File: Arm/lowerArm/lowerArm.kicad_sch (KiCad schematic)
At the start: 4 parts, among them J1 Screw_Terminal_01x12, J2 Screw_Terminal_01x12, U1 LM1084-5.0

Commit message: updated Arm arduino code, manual_operate, and PCBs
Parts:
- added C1: 0.1uF, Capacitor_SMD:C_0805_2012Metric, symbol Device:C_Small
- added C2, C3: 22pF, Capacitor_SMD:C_0805_2012Metric, symbol Device:C_Small
- added D?: LED, symbol Device:LED
- added J3: Screw_Terminal_01x02, TerminalBlock_4Ucon:TerminalBlock_4Ucon_1x02_P3.50mm_Horizontal, symbol Connector:Screw_Terminal_01x02
- added R1, R2: 1k, Resistor_SMD:R_0805_2012Metric, symbol Device:R_US
- added R3: R_US, Resistor_SMD:R_0805_2012Metric, symbol Device:R_US
- added U2: Crystal_Oscillator_8MHz, LFXTAL:LFXTAL057135Bulk, symbol customSymbols:Crystal_Oscillator_8MHz
- added U3: MCP2515-xSO, MCP2515_SMD:SOIC127P1030X265-18N, symbol Interface_CAN_LIN:MCP2515-xSO
- added U4: MAX3051, MAX3051:SOIC127P600X175-8N, symbol Interface_UART:MAX3051
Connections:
- net GND: now also C1.1, C2.2, C3.2, R1.2, U3.9 (VSS), U4.2 (GND)
- net at J2.1 (Pin_1): no longer A1.17 (3V3)
- net at J1.1 (Pin_1): no longer A1.5 (D2)
- net at J1.10 (Pin_10): no longer A1.14 (D11)
- net at J1.11 (Pin_11): no longer A1.15 (D12)
- net at J1.9 (Pin_9): no longer A1.13 (D10)
- net at A1.16 (D13): now also U3.13 (SCK)
- new net: R2.1, U3.17 (~{RESET})
- new net: A1.17 (3V3), C1.2, R2.2, U3.18 (VDD), U4.3 (VDD)
- new net: C3.1, U2.2, U3.8 (OSC1)
- new net: C2.1, U2.1, U3.7 (OSC2)
- new net: A1.13 (D10), U3.16 (~{CS})
- new net: A1.14 (D11), U3.14 (SI)
- new net: A1.15 (D12), U3.15 (SO)
- new net: U3.2 (RXCAN), U4.1 (TXD)
- new net: U3.1 (TXCAN), U4.4 (RXD)
- new net: J3.2 (Pin_2), R3.2, U4.6 (CANL)
- new net: J3.1 (Pin_1), R3.1, U4.7 (CANH)
- new net: R1.1, U4.8 (RS)
- no-connect marks 0 -> 6
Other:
- moved on the sheet: J1

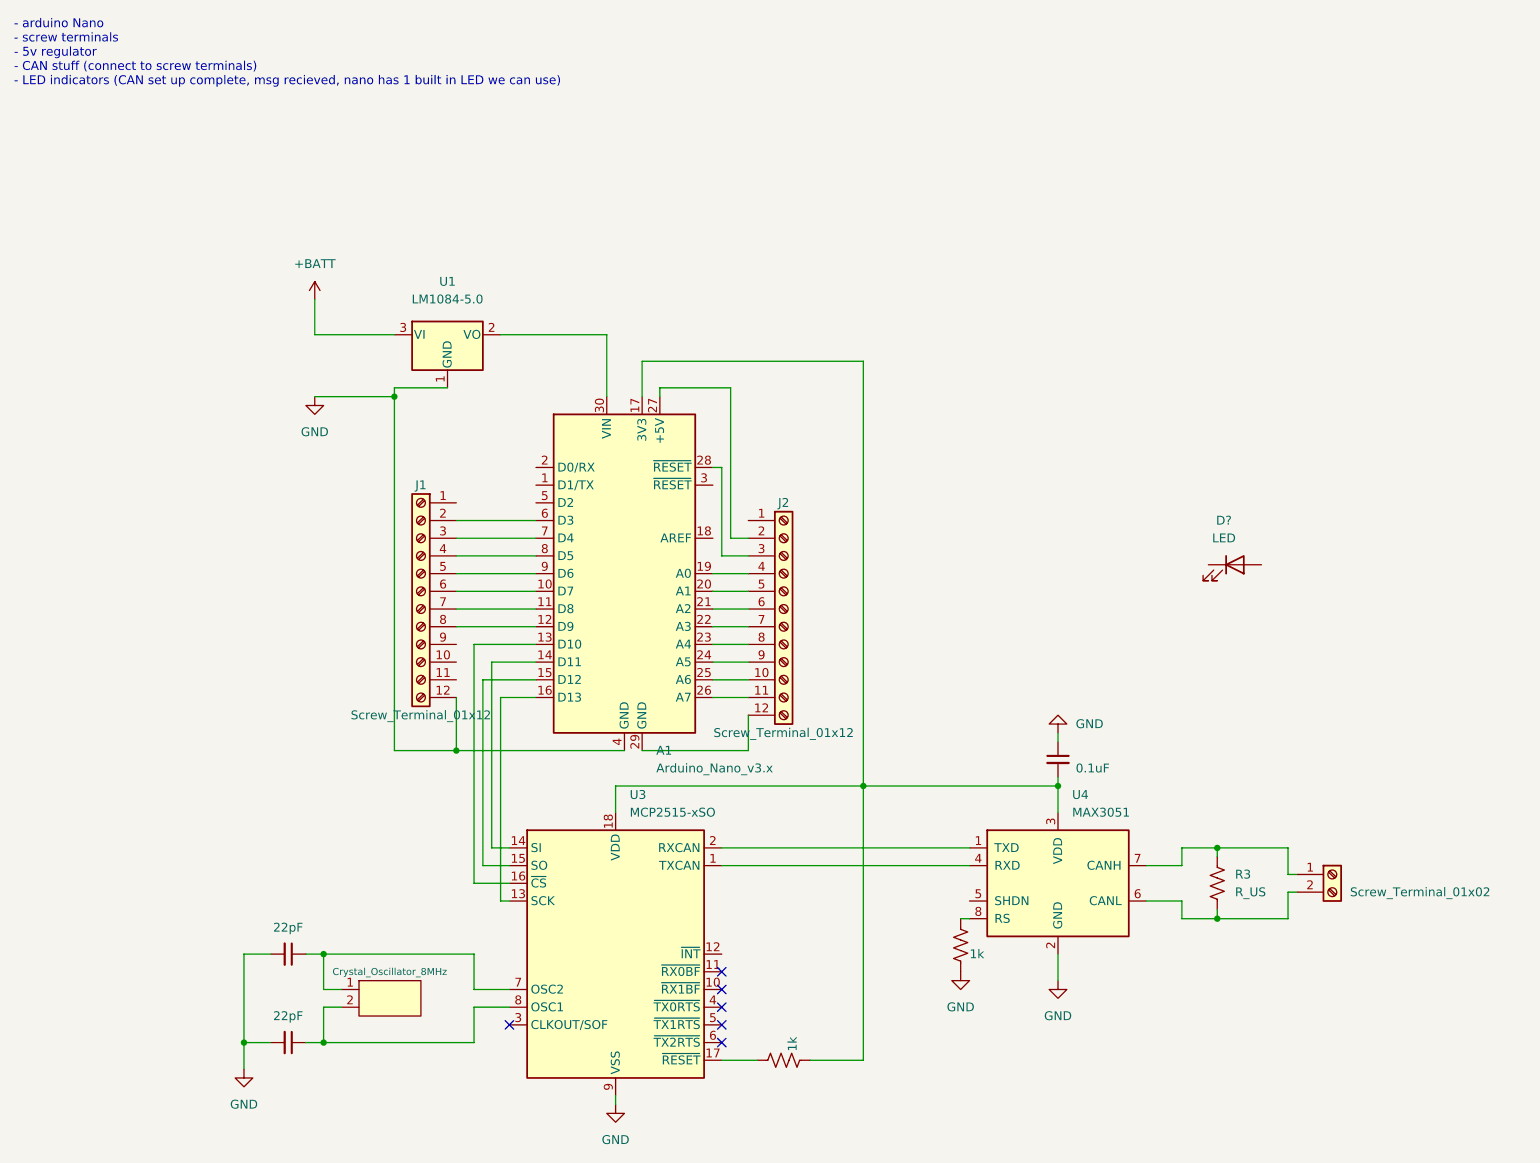
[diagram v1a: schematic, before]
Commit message: Updated wheel code, organized, added a folder for examples I'vemade
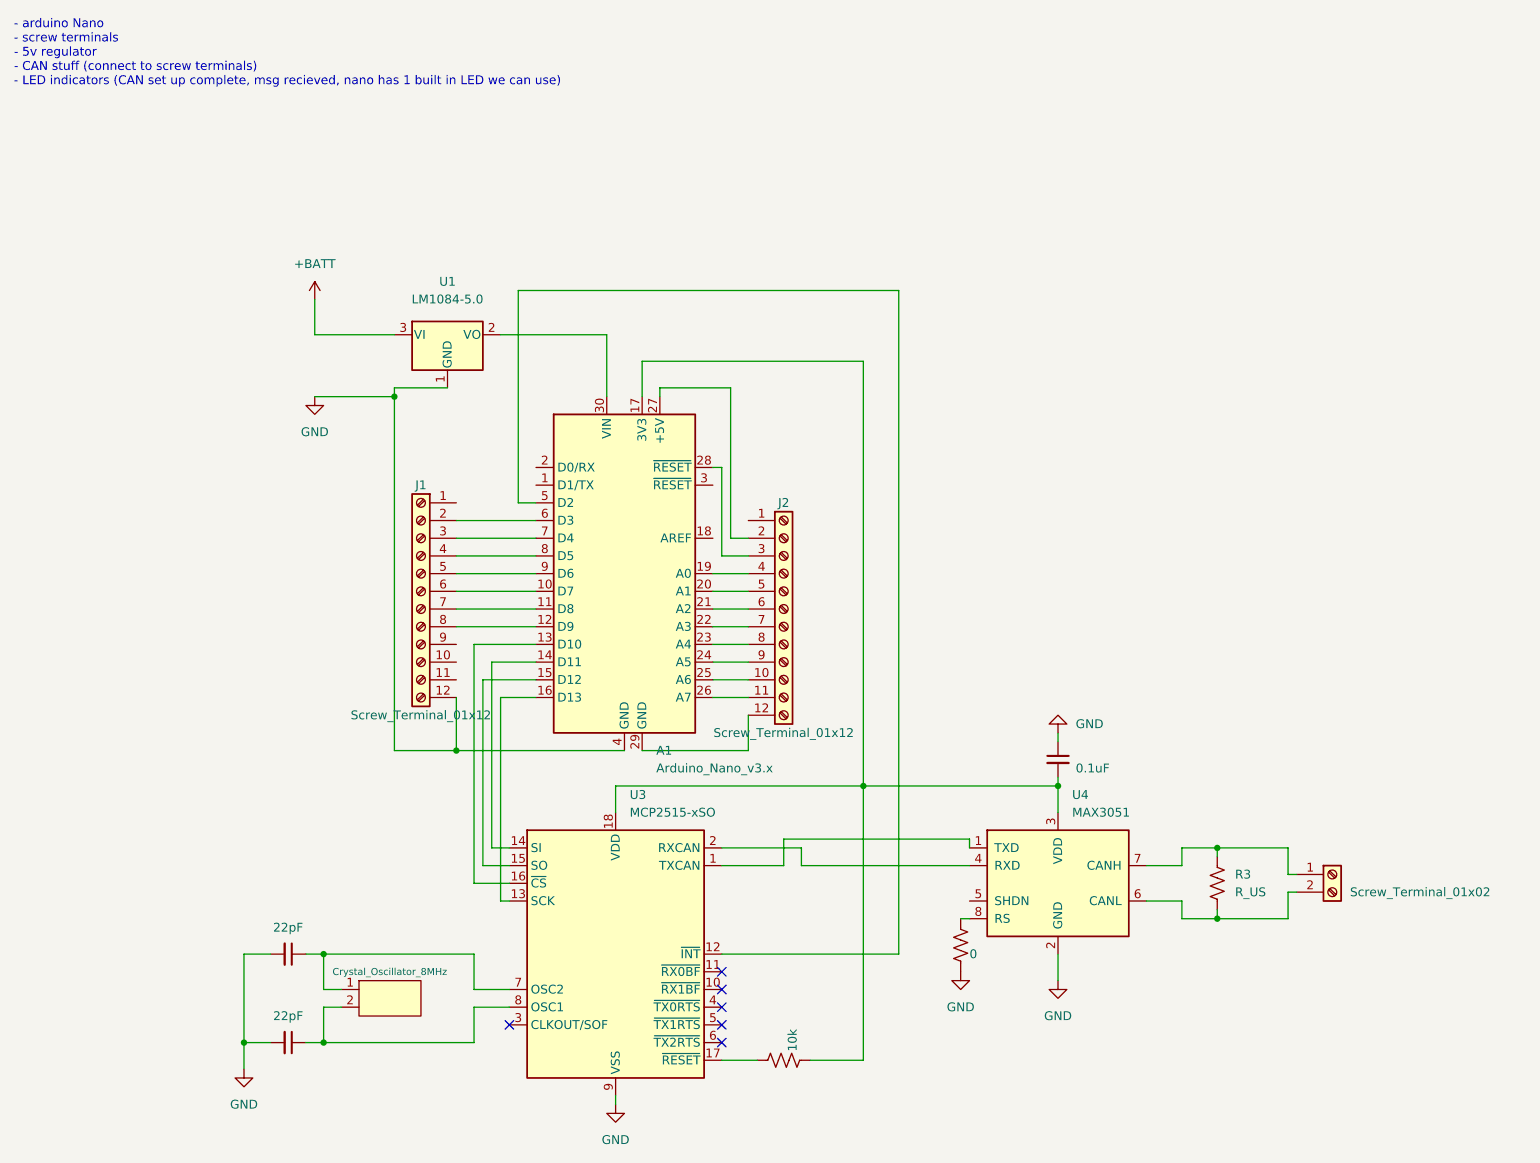
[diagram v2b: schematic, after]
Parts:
- removed D?: LED, symbol Device:LED
- R1: value 1k -> 0
- R2: value 1k -> 10k
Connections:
- net at A1.5 (D2): now also U3.12 (~{INT})
- net at U4.1 (TXD): now also U3.1 (TXCAN); no longer U3.2 (RXCAN)
- net at U4.4 (RXD): now also U3.2 (RXCAN); no longer U3.1 (TXCAN)
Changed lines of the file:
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@@
+    (stroke (width 0) (type default) (color 0 0 0 0))
+  )
+  (wire (pts (xy 152.4 137.16) (xy 128.27 137.16))
     (stroke (width 0) (type default) (color 0 0 0 0))
   )
@@
     (stroke (width 0) (type default) (color 0 0 0 0))
   )
+  (wire (pts (xy 128.27 134.62) (xy 116.84 134.62))
+    (stroke (width 0) (type default) (color 0 0 0 0))
+  )
   (wire (pts (xy 107.95 68.58) (xy 118.11 68.58))
     (stroke (width 0) (type default) (color 0 0 0 0))
@@
     (stroke (width 0) (type default) (color 0 0 0 0))
   )
+  (wire (pts (xy 128.27 137.16) (xy 128.27 134.62))
+    (stroke (width 0) (type default) (color 0 0 0 0))
+  )
   (wire (pts (xy 82.55 137.16) (xy 82.55 110.49))
     (stroke (width 0) (type default) (color 0 0 0 0))
@@
     (stroke (width 0) (type default) (color 0 0 0 0))
   )
-  (wire (pts (xy 116.84 134.62) (xy 152.4 134.62))
-    (stroke (width 0) (type default) (color 0 0 0 0))
-  )
   (wire (pts (xy 199.39 138.43) (xy 198.12 138.43))
     (stroke (width 0) (type default) (color 0 0 0 0))
@@
     (stroke (width 0) (type default) (color 0 0 0 0))
   )
+  (wire (pts (xy 142.24 54.61) (xy 87.63 54.61))
+    (stroke (width 0) (type default) (color 0 0 0 0))
+  )
+  (wire (pts (xy 125.73 133.35) (xy 152.4 133.35))
+    (stroke (width 0) (type default) (color 0 0 0 0))
+  )
   (wire (pts (xy 81.28 149.86) (xy 81.28 154.94))
     (stroke (width 0) (type default) (color 0 0 0 0))
   )
-  (wire (pts (xy 116.84 137.16) (xy 152.4 137.16))
-    (stroke (width 0) (type default) (color 0 0 0 0))
-  )
   (wire (pts (xy 165.1 153.67) (xy 165.1 149.86))
     (stroke (width 0) (type default) (color 0 0 0 0))
   )
+  (wire (pts (xy 116.84 149.86) (xy 142.24 149.86))
+    (stroke (width 0) (type default) (color 0 0 0 0))
+  )
+  (wire (pts (xy 87.63 54.61) (xy 87.63 85.09))
+    (stroke (width 0) (type default) (color 0 0 0 0))
+  )
   (wire (pts (xy 182.88 142.24) (xy 182.88 144.78))
     (stroke (width 0) (type default) (color 0 0 0 0))
@@
     (stroke (width 0) (type default) (color 0 0 0 0))
   )
+  (wire (pts (xy 116.84 137.16) (xy 125.73 137.16))
+    (stroke (width 0) (type default) (color 0 0 0 0))
+  )
   (wire (pts (xy 165.1 125.73) (xy 165.1 129.54))
     (stroke (width 0) (type default) (color 0 0 0 0))
@@
     (stroke (width 0) (type default) (color 0 0 0 0))
   )
+  (wire (pts (xy 87.63 85.09) (xy 90.17 85.09))
+    (stroke (width 0) (type default) (color 0 0 0 0))
+  )
   (wire (pts (xy 120.65 120.65) (xy 120.65 115.57))
     (stroke (width 0) (type default) (color 0 0 0 0))
@@
     (stroke (width 0) (type default) (color 0 0 0 0))
   )
+  (wire (pts (xy 152.4 133.35) (xy 152.4 134.62))
+    (stroke (width 0) (type default) (color 0 0 0 0))
+  )
   (wire (pts (xy 115.57 102.87) (xy 120.65 102.87))
     (stroke (width 0) (type default) (color 0 0 0 0))
@@
     (stroke (width 0) (type default) (color 0 0 0 0))
   )
+  (wire (pts (xy 142.24 149.86) (xy 142.24 54.61))
+    (stroke (width 0) (type default) (color 0 0 0 0))
+  )
   (wire (pts (xy 69.85 69.85) (xy 69.85 68.58))
     (stroke (width 0) (type default) (color 0 0 0 0))
@@
   )
   (wire (pts (xy 78.74 102.87) (xy 90.17 102.87))
+    (stroke (width 0) (type default) (color 0 0 0 0))
+  )
+  (wire (pts (xy 125.73 137.16) (xy 125.73 133.35))
     (stroke (width 0) (type default) (color 0 0 0 0))
   )
@@
       (effects (font (size 1.27 1.27)) (justify left) hide)
     )
-    (property "Value" "1k" (id 1) (at 127 163.83 0)
+    (property "Value" "10k" (id 1) (at 127 163.83 0)
       (effects (font (size 1.27 1.27)) (justify left))
     )
@@
     (pin "2")
     (pin "3")
-  )
-  (symbol (lib_id "Device:LED") (at 190.5 93.98 0) (unit 1)
-    (in_bom yes) (on_board yes) (fields_autoplaced)
-    (property "Reference" "D?" (id 0) (at 188.9125 87.63 0))
-    (property "Value" "LED" (id 1) (at 188.9125 90.17 0))
-    (property "Footprint" "" (id 2) (at 190.5 93.98 0)
-      (effects (font (size 1.27 1.27)) hide)
-    )
-    (property "Datasheet" "~" (id 3) (at 190.5 93.98 0)
-      (effects (font (size 1.27 1.27)) hide)
-    )
-    (pin "1")
-    (pin "2")
   )
   (symbol (lib_id "MCU_Module:Arduino_Nano_v3.x") (at 102.87 95.25 0) (unit 1)
@@
       (effects (font (size 1.27 1.27)) (justify left) hide)
     )
-    (property "Value" "1k" (id 1) (at 152.4 149.86 0)
+    (property "Value" "0" (id 1) (at 152.4 149.86 0)
       (effects (font (size 1.27 1.27)) (justify left))
     )
@@
       (reference "C3") (unit 1) (value "22pF") (footprint "Capacitor_SMD:C_0805_2012Metric")
     )
-    (path "/5321996d-b27f-4508-a4f3-7f01cfc2d729"
-      (reference "D?") (unit 1) (value "LED") (footprint "")
-    )
     (path "/40a5cd71-b559-4b39-b4a6-eb52ab9b18cc"
       (reference "J1") (unit 1) (value "Screw_Terminal_01x12") (footprint "TerminalBlock_4Ucon:TerminalBlock_4Ucon_1x12_P3.50mm_Horizontal")
@@
     )
     (path "/d9e78932-399f-440e-9289-b3c405aef8c8"
-      (reference "R1") (unit 1) (value "1k") (footprint "Resistor_SMD:R_0805_2012Metric")
+      (reference "R1") (unit 1) (value "0") (footprint "Resistor_SMD:R_0805_2012Metric")
     )
     (path "/3680ecf3-6714-42e2-b97b-9aff83bb81cb"
-      (reference "R2") (unit 1) (value "1k") (footprint "Resistor_SMD:R_0805_2012Metric")
+      (reference "R2") (unit 1) (value "10k") (footprint "Resistor_SMD:R_0805_2012Metric")
     )
     (path "/b3df2273-0303-4576-9343-0c8a734974c2"
